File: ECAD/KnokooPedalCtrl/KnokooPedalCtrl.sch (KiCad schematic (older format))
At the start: 19 parts, among them J1 MAIN PCB CONNECTION, J2 Conn_01x04, J3 UI, J5 ICSP, U2 PIC12F1572

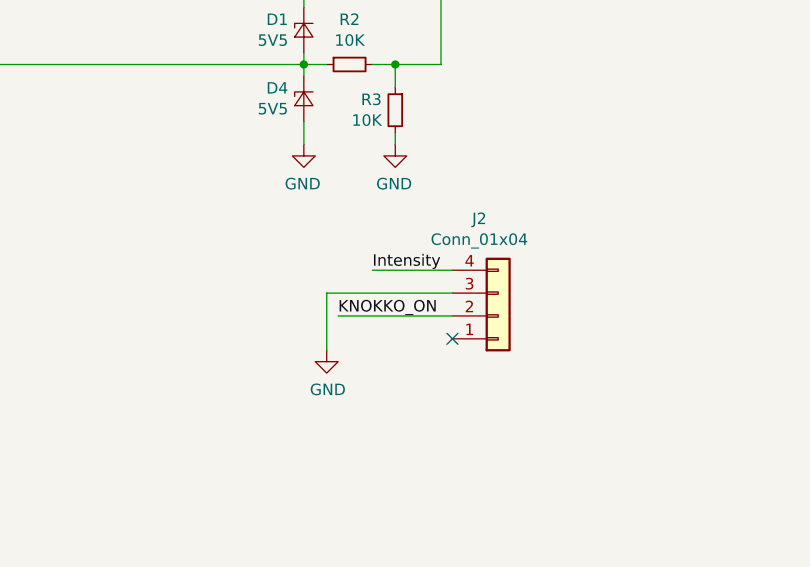
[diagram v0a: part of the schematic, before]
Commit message: v0.1
Small pinout and silkscreen fixes
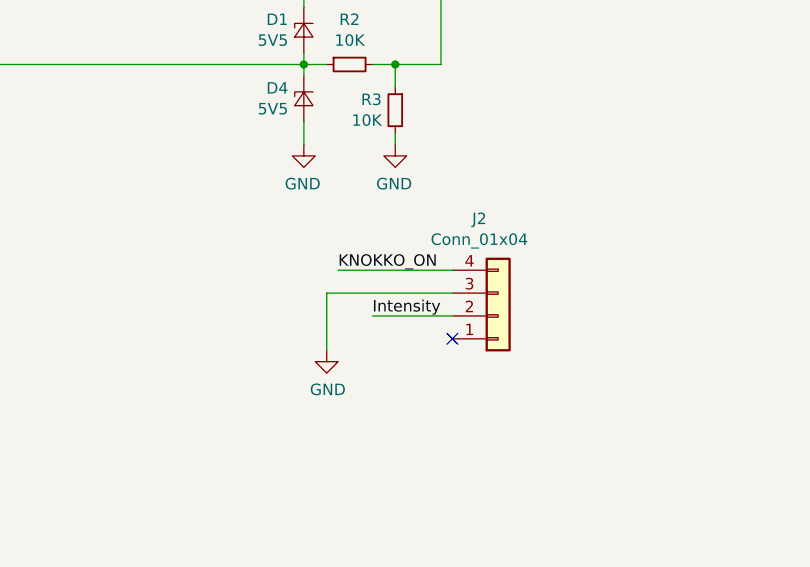
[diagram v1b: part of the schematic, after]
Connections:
- net Intensity: now also J2.2 (Pin_2); no longer J2.4 (Pin_4)
- net KNOKKO_ON: now also J2.4 (Pin_4); no longer J2.2 (Pin_2)
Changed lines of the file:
@@
 Sheet 1 1
 Title "Knokoo Pedal Mod"
-Date "2020-09-26"
-Rev "v0.0"
+Date "2020-10-17"
+Rev "v0.1"
 Comp "Philipp Schilk"
 Comment1 ""
@@
 Wire Wire Line
 	3100 5000 3400 5000
-Text Label 7500 4800 0    50   ~ 0
+Text Label 7500 5000 0    50   ~ 0
 Intensity
 Wire Wire Line
-	7850 4800 7500 4800
+	7850 5000 7500 5000
 Wire Wire Line
 	7850 4900 7300 4900
@@
 Text Label 5500 3000 2    50   ~ 0
 KNOKKO_ON
-Text Label 7350 5000 0    50   ~ 0
+Text Label 7350 4800 0    50   ~ 0
 KNOKKO_ON
 Wire Wire Line
-	7350 5000 7850 5000
+	7350 4800 7850 4800
 Wire Wire Line
 	2900 2900 3900 2900

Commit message: v0.2
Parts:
- added R6, R7: DNS, Resistor_SMD:R_0603_1608Metric, symbol Device:R_Small
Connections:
- net +5V: now also R6.1
- net Duration_Sense: now also R6.2, R7.1
- net GND: now also R7.2
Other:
- note added: "R6/R7 May be used instead of a second\nPotentiometer to fix the timer duration."
- moved on the sheet: H1, H2
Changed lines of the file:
@@
 Sheet 1 1
 Title "Knokoo Pedal Mod"
-Date "2020-10-17"
-Rev "v0.1"
+Date "2020-11-01"
+Rev "v0.2"
 Comp "Philipp Schilk"
 Comment1 ""
 Comment2 ""
 Comment3 ""
-Comment4 ""
+Comment4 "https://github.com/TheSchilk/KnokooPedalCtrl"
 $EndDescr
 $Comp
@@
 Text Label 7200 1500 0    50   ~ 0
 LED
-Text Label 7200 1400 0    50   ~ 0
+Text Label 6050 1400 0    50   ~ 0
 Duration_Sense
-Wire Wire Line
-	7200 1400 7950 1400
 $Comp
 L Device:R_Small R1
@@
 L Mechanical:MountingHole H1
 U 1 1 5F86627B
-P 3300 6100
-F 0 "H1" H 3400 6146 50  0000 L CNN
-F 1 "MountingHole" H 3400 6055 50  0000 L CNN
-F 2 "MountingHole:MountingHole_3.2mm_M3_Pad_Via" H 3300 6100 50  0001 C CNN
-F 3 "~" H 3300 6100 50  0001 C CNN
-	1    3300 6100
+P 4350 4800
+F 0 "H1" H 4450 4846 50  0000 L CNN
+F 1 "MountingHole" H 4450 4755 50  0000 L CNN
+F 2 "MountingHole:MountingHole_3.2mm_M3_Pad_Via" H 4350 4800 50  0001 C CNN
+F 3 "~" H 4350 4800 50  0001 C CNN
+	1    4350 4800
 	1    0    0    -1
 $EndComp
@@
 L Mechanical:MountingHole H2
 U 1 1 5F869A83
-P 3300 6400
-F 0 "H2" H 3400 6446 50  0000 L CNN
-F 1 "MountingHole" H 3400 6355 50  0000 L CNN
-F 2 "MountingHole:MountingHole_3.2mm_M3_Pad_Via" H 3300 6400 50  0001 C CNN
-F 3 "~" H 3300 6400 50  0001 C CNN
-	1    3300 6400
+P 4350 5100
+F 0 "H2" H 4450 5146 50  0000 L CNN
+F 1 "MountingHole" H 4450 5055 50  0000 L CNN
+F 2 "MountingHole:MountingHole_3.2mm_M3_Pad_Via" H 4350 5100 50  0001 C CNN
+F 3 "~" H 4350 5100 50  0001 C CNN
+	1    4350 5100
 	1    0    0    -1
 $EndComp
@@
 	-1   0    0    1
 $EndComp
+Wire Wire Line
+	6050 1400 6800 1400
+$Comp
+L Device:R_Small R7
+U 1 1 5F9F03FE
+P 6800 1600
+F 0 "R7" H 6859 1646 50  0000 L CNN
+F 1 "DNS" H 6859 1555 50  0000 L CNN
+F 2 "Resistor_SMD:R_0603_1608Metric" H 6800 1600 50  0001 C CNN
+F 3 "~" H 6800 1600 50  0001 C CNN
+	1    6800 1600
+	-1   0    0    -1
+$EndComp
+$Comp
+L Device:R_Small R6
+U 1 1 5F9F0733
+P 6800 1200
+F 0 "R6" H 6859 1246 50  0000 L CNN
+F 1 "DNS" H 6859 1155 50  0000 L CNN
+F 2 "Resistor_SMD:R_0603_1608Metric" H 6800 1200 50  0001 C CNN
+F 3 "~" H 6800 1200 50  0001 C CNN
+	1    6800 1200
+	-1   0    0    -1
+$EndComp
+Wire Wire Line
+	6800 1500 6800 1400
+Connection ~ 6800 1400
+Wire Wire Line
+	6800 1400 7950 1400
+Wire Wire Line
+	6800 1400 6800 1300
+Wire Wire Line
+	6800 1100 6800 1050
+$Comp
+L power:+5V #PWR0120
+U 1 1 5F9FC84C
+P 6800 1050
+F 0 "#PWR0120" H 6800 900 50  0001 C CNN
+F 1 "+5V" H 6815 1223 50  0000 C CNN
+F 2 "" H 6800 1050 50  0001 C CNN
+F 3 "" H 6800 1050 50  0001 C CNN
+	1    6800 1050
+	-1   0    0    -1
+$EndComp
+$Comp
+L power:GND #PWR0121
+U 1 1 5F9FE8F3
+P 6800 1800
+F 0 "#PWR0121" H 6800 1550 50  0001 C CNN
+F 1 "GND" H 6800 1600 50  0000 C CNN
+F 2 "" H 6800 1800 50  0001 C CNN
+F 3 "" H 6800 1800 50  0001 C CNN
+	1    6800 1800
+	-1   0    0    -1
+$EndComp
+Wire Wire Line
+	6800 1800 6800 1700
+Text Notes 6150 750  0    50   ~ 0
+R6/R7 May be used instead of a second\nPotentiometer to fix the timer duration.
 $EndSCHEMATC
